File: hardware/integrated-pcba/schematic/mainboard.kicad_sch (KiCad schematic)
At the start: 64 parts, among them J1 USB-C USB2 receptacle, J2 1S protected battery + 10k NTC, Q1 MMBT3904, Q2 MMBT3904, Q3 MMBT3904, Q4 MMBT3904, SW1 RESET push button, SW2 DICTATE / BOOT push button, SW3 RUN SPDT slide, U1 ESP32-WROOM-32E-N4, U2 INMP441, U3 CP2102N-A02-GQFN28, U4 SN74LVC2G125DCUR, U5 SN74LVC2G125DCUR, U6 SN74LVC2G125DCUR, U7 BQ24075RGTR, U8 TPS63070RNMR

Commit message: hardware: migrate electrical draft to LCEDA Pro and quote one board
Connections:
- net GND: no longer SW3.3 (OFF)
- no-connect marks 51 -> 52
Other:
- moved on the sheet: C1, C10, C11, C12, C13, C14, C15, C16, C17, C18, C19, C2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

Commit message: 完成整板封装绑定及原生 PCB 初步布局
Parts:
- U3: footprint Package_DFN_QFN:QFN-28-1EP_5x5mm_P0.5mm_EP3.35x3.35mm -> VOXU:VOXU_CP2102N_QFN28
- U7: footprint Package_DFN_QFN:VQFN-16-1EP_3x3mm_P0.5mm_EP1.45x1.45mm -> VOXU:VOXU_BQ24075_RGT0016C

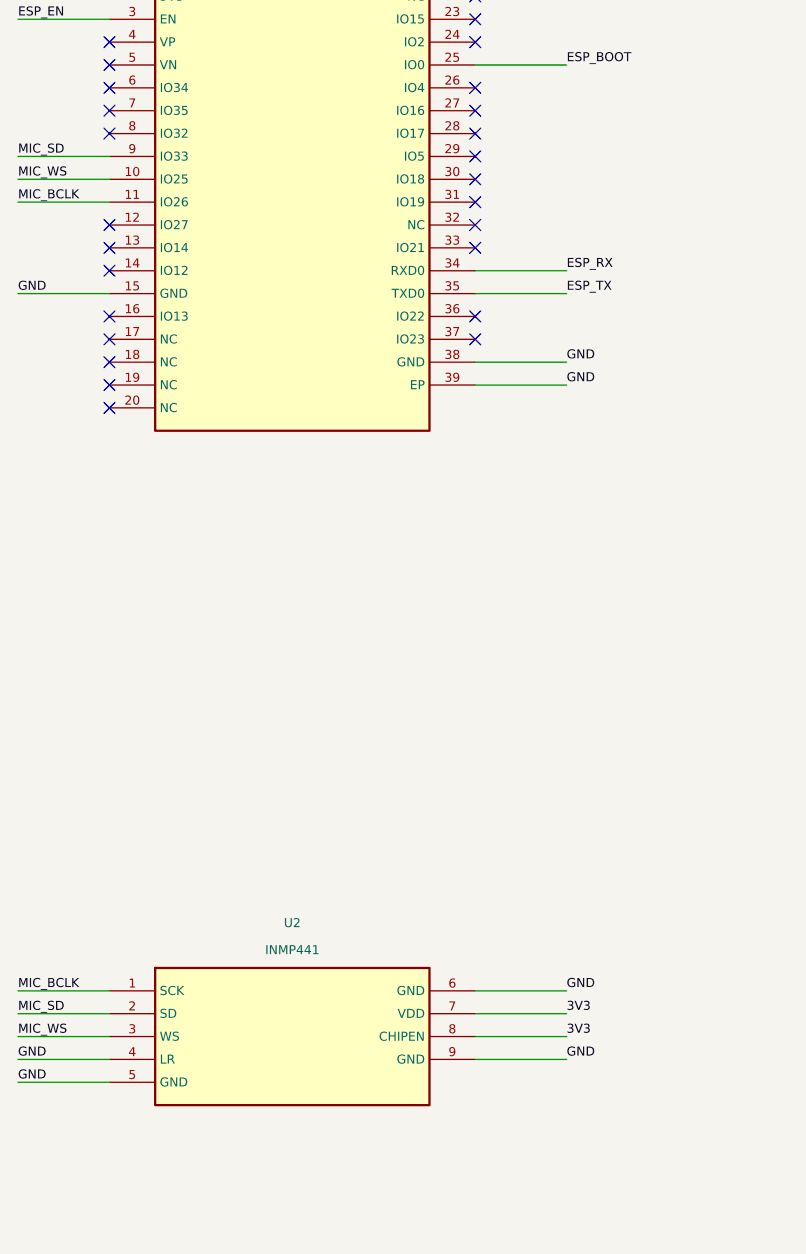
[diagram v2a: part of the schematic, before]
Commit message: 替换现货 SPH0655 麦克风并完成紧凑主板布线检查
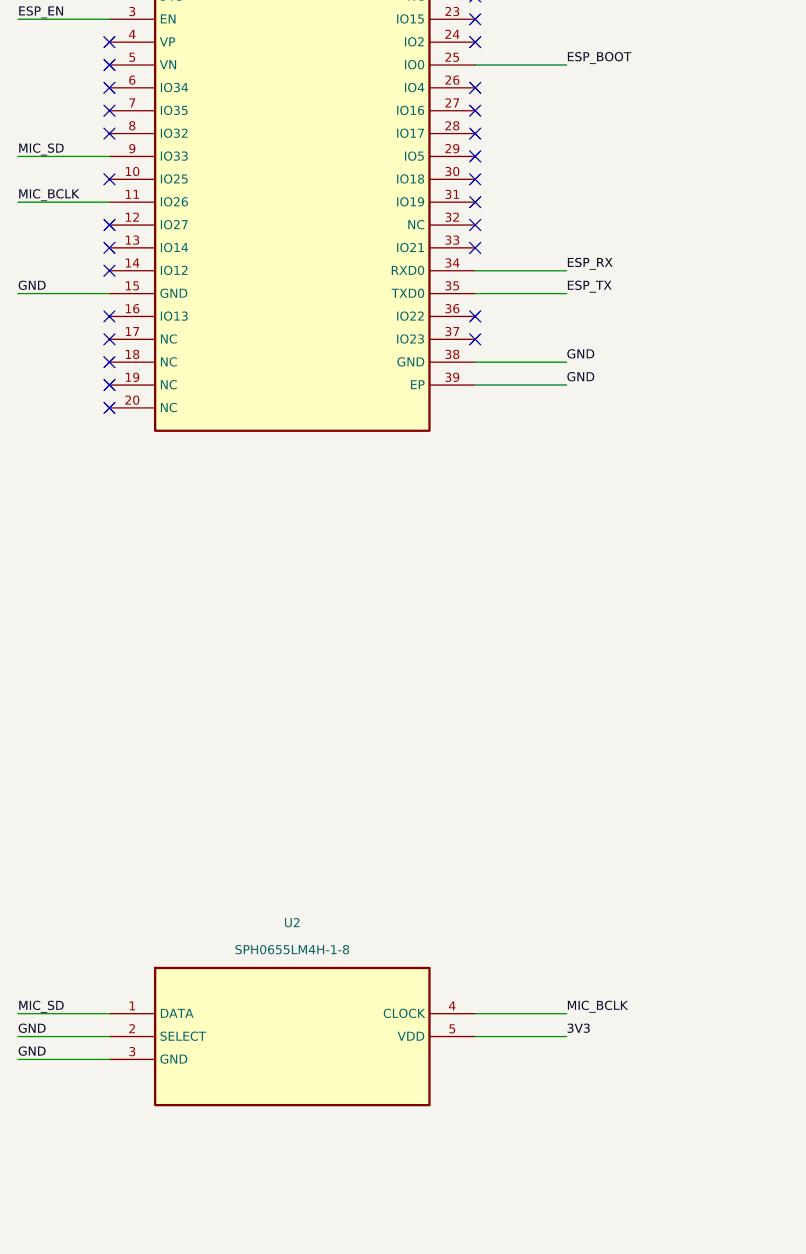
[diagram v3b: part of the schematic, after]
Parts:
- U2: value INMP441 -> SPH0655LM4H-1-8; footprint (none) -> MIC-SMD_SPH0655LM4H-1-8; LCSC C5438445 -> C22376158
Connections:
- net 3V3: now also U2.5 (VDD); no longer U2.7 (VDD), U2.8 (CHIPEN)
- net GND: now also U2.2 (SELECT), U2.3 (GND); no longer U2.4 (LR), U2.5 (GND), U2.6 (GND), U2.9 (GND)
- net MIC_BCLK: now also U2.4 (CLOCK); no longer U2.1 (SCK)
- net MIC_SD: now also U2.1 (DATA); no longer U2.2 (SD)
- net MIC_WS: no longer names the net of U1.10 (IO25)
- net MIC_WS: no longer U2.3 (WS)
- no-connect marks 52 -> 53
